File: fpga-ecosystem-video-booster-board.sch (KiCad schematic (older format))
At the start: 46 parts

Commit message: LED and I2C input option added. Annotated sch.
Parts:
- added D1: LG_L29K-G2J1-24-Z, antmicro-footprints:LED_0603, symbol antmicroLEDIndicationDiscrete:LG_L29K-G2J1-24-Z
- added R11, R12: R_15R_0402, antmicro-footprints:0402-res, symbol antmicroResistors0402:R_15R_0402
- added R4: R_330R_0402, antmicro-footprints:0402-res, symbol antmicroResistors0402:R_330R_0402
- gave numbers to parts that had none: 46
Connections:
- net labels added: SCL_MCU, SDA_MCU
- wire segments 219 -> 230
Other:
- note added: "SWD Debug"
- moved on the sheet: C1, C10, C11, C12, C13, C14, C15, C16, C17, C18, C19, C2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

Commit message: PCB update issues solved. PTN gnd connection fix
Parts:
- removed J2: HDMI_A, symbol Connector:HDMI_A
- removed J6: 685119134923, antmicro-footprints:685119134923, symbol antmicroUSBDVIHDMIConnectors:685119134923
- added J2: HDMI-PE10-19-LF, antmicro-footprints:HDMI-PE10-19-LF, symbol antmicroUSBDVIHDMIConnectors:HDMI-PE10-19-LF
- added J6: 685119134923_, antmicro-footprints:HDMI_A_Female_685119134923, symbol antmicroUSBDVIHDMIConnectors:685119134923_
- J3: footprint antmicro-footprints:PinHeader_1x4_P2.54_Drill1.1mm -> antmicro-footprints:PinHeader_1x4_P2.54mm_Drill1.02mm
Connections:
- wire segments 230 -> 238
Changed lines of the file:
@@
 Comment4 ""
 $EndDescr
-$Comp
-L Connector:HDMI_A J2
-U 1 1 5DB0BA68
-P 1650 3450
-F 0 "J2" H 2080 3496 50  0000 L CNN
-F 1 "HDMI_A" H 2080 3405 50  0000 L CNN
-F 2 "" H 1675 3450 50  0001 C CNN
-F 3 "https://en.wikipedia.org/wiki/HDMI" H 1675 3450 50  0001 C CNN
-	1    1650 3450
-	-1   0    0    -1
-$EndComp
-Text Notes 1000 3050 1    50   ~ 0
+Text Notes 1200 3400 1    50   ~ 0
 Generic\nShoud be male plus, such as \nSamtec HDMP-19-01-S-EM\nMorethanall HDMI-PE10-19-LF\n
-$Comp
-L antmicroUSBDVIHDMIConnectors:685119134923 J6
-U 1 1 5DB15BF1
-P 9400 3450
-F 0 "J6" H 9830 3496 50  0000 L CNN
-F 1 "685119134923" H 9830 3405 50  0000 L CNN
-F 2 "antmicro-footprints:685119134923" H 9425 3450 50  0001 C CNN
-F 3 "https://en.wikipedia.org/wiki/HDMI" H 9425 3450 50  0001 C CNN
-	1    9400 3450
-	1    0    0    -1
-$EndComp
-$Comp
-L antmicroInterfaceDriversReceiversTransceivers:PTN3363 U3
-U 1 1 5DB15F6D
-P 5800 3250
-F 0 "U3" H 5400 4300 60  0000 C CNN
-F 1 "PTN3363" H 6100 4300 60  0000 C CNN
-F 2 "antmicro-footprints:QFN-32-1EP_5x5mm" H 4900 1450 60  0001 L CNN
-F 3 "https://www.nxp.com/docs/en/data-sheet/PTN3363.pdf" H 4550 1350 60  0001 L CNN
-F 4 "NXP" H 5300 1550 60  0001 L CNN "Manufacturer"
-F 5 "PTN3363" H 5550 1550 60  0001 L CNN "MPN"
-	1    5800 3250
-	1    0    0    -1
-$EndComp
 $Comp
 L antmicroCapacitors0402:C_100n_0402_6V3 C12
@@
 Wire Wire Line
 	2050 2950 2950 2950
-Wire Wire Line
-	3350 3350 2050 3350
 Text Label 2150 2650 0    50   ~ 0
 IN_D2_P
@@
 	3350 3350 3350 3650
 Wire Wire Line
-	3350 3650 3950 3650
+	3350 3650 3400 3650
 Text Label 8500 2650 0    50   ~ 0
 OUT_D2_P
@@
 Wire Wire Line
 	5700 1550 5350 1550
-Wire Wire Line
-	2050 3050 3050 3050
 Wire Wire Line
 	2050 3550 2400 3550
@@
 	3250 2500 3250 3250
 Wire Wire Line
-	2050 3250 3250 3250
+	2050 3250 3000 3250
 Connection ~ 3250 3250
 Wire Wire Line
@@
 F 0 "J3" V 4541 6873 50  0000 R CNN
 F 1 "61300411121" V 4450 6873 50  0000 R CNN
-F 2 "antmicro-footprints:PinHeader_1x4_P2.54_Drill1.1mm" H 4550 7150 60  0001 L CNN
+F 2 "antmicro-footprints:PinHeader_1x4_P2.54mm_Drill1.02mm" H 4550 7150 60  0001 L CNN
 F 3 "https://katalog.we-online.de/em/datasheet/6130xx11121.pdf" H 4550 7250 60  0001 L CNN
 F 4 "61300411121" H 4550 7450 60  0001 L CNN "MPN"
@@
 	-1   0    0    -1
 $EndComp
-Wire Wire Line
-	2550 5650 2550 5750
 Connection ~ 2550 5650
 Wire Wire Line
@@
 Text Label 6200 7500 0    50   ~ 0
 SDA_SRC
+Wire Wire Line
+	2050 3350 3350 3350
+Wire Wire Line
+	2050 3050 3050 3050
+Wire Wire Line
+	2550 5650 2550 5750
+Connection ~ 2550 5750
+Wire Wire Line
+	2550 5750 2550 5850
+Connection ~ 2550 5850
+Wire Wire Line
+	2550 5850 2550 5950
+Connection ~ 2550 5950
+Wire Wire Line
+	2550 5950 2550 6050
+$Comp
+L antmicroInterfaceDriversReceiversTransceivers:PTN3363 U3
+U 1 1 5DB5B52F
+P 5800 3250
+F 0 "U3" H 5450 4300 60  0000 C CNN
+F 1 "PTN3363" H 6100 4300 60  0000 C CNN
+F 2 "antmicro-footprints:QFN-32-1EP_5x5mm" H 4900 1450 60  0001 L CNN
+F 3 "https://www.nxp.com/docs/en/data-sheet/PTN3363.pdf" H 4550 1350 60  0001 L CNN
+F 4 "NXP" H 5300 1550 60  0001 L CNN "Manufacturer"
+F 5 "PTN3363" H 5550 1550 60  0001 L CNN "MPN"
+	1    5800 3250
+	1    0    0    -1
+$EndComp
+$Comp
+L power:GND #PWR?
+U 1 1 5DB5B819
+P 6600 2450
+F 0 "#PWR?" H 6600 2200 50  0001 C CNN
+F 1 "GND" H 6605 2277 50  0000 C CNN
+F 2 "" H 6600 2450 50  0001 C CNN
+F 3 "" H 6600 2450 50  0001 C CNN
+	1    6600 2450
+	1    0    0    -1
+$EndComp
+Wire Wire Line
+	6400 2450 6600 2450
+Wire Wire Line
+	6600 2450 6600 2350
+Wire Wire Line
+	6600 2350 6400 2350
+Connection ~ 6600 2450
+$Comp
+L antmicroUSBDVIHDMIConnectors:HDMI-PE10-19-LF J2
+U 1 1 5DBAED87
+P 1550 3600
+F 0 "J2" V 1100 2850 50  0000 R CNN
+F 1 "HDMI-PE10-19-LF" V 1200 3500 50  0000 R CNN
+F 2 "antmicro-footprints:HDMI-PE10-19-LF" H 1750 3800 60  0001 L CNN
+F 3 "http://www.morethanall.com/images/products/March2017/JtPYSqVaIFqwSbTYDg6j.pdf" H 1625 3750 50  0001 C CNN
+	1    1550 3600
+	1    0    0    -1
+$EndComp
+Connection ~ 3000 3250
+Wire Wire Line
+	3000 3250 3250 3250
+Connection ~ 3400 3650
+Wire Wire Line
+	3400 3650 3950 3650
+$Comp
+L antmicroUSBDVIHDMIConnectors:685119134923_ J6
+U 1 1 5DBAFB0A
+P 9400 3450
+F 0 "J6" H 9150 4500 50  0000 L CNN
+F 1 "685119134923_" V 9900 2500 50  0000 L CNN
+F 2 "antmicro-footprints:HDMI_A_Female_685119134923" H 9600 3650 60  0001 L CNN
+F 3 "https://katalog.we-online.de/em/datasheet/685119134923.pdf" H 9425 3450 50  0001 C CNN
+	1    9400 3450
+	1    0    0    -1
+$EndComp
 $EndSCHEMATC

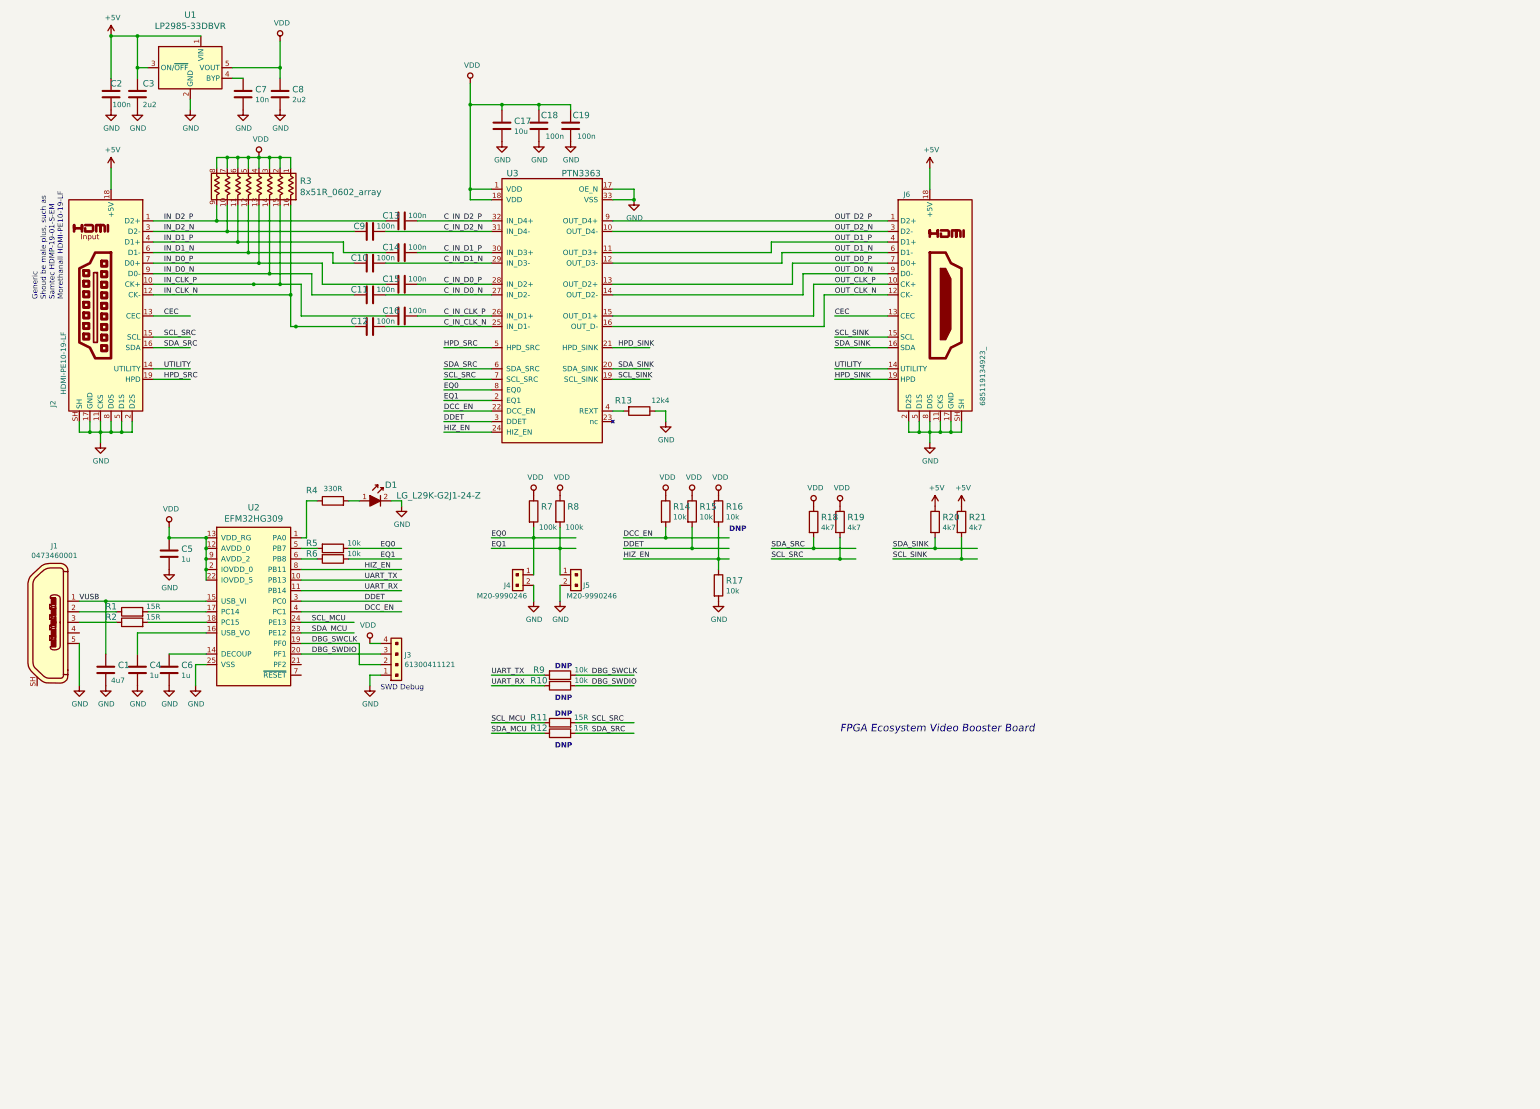
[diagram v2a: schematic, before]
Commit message: Schematics with two channels. I2Cs connected directly
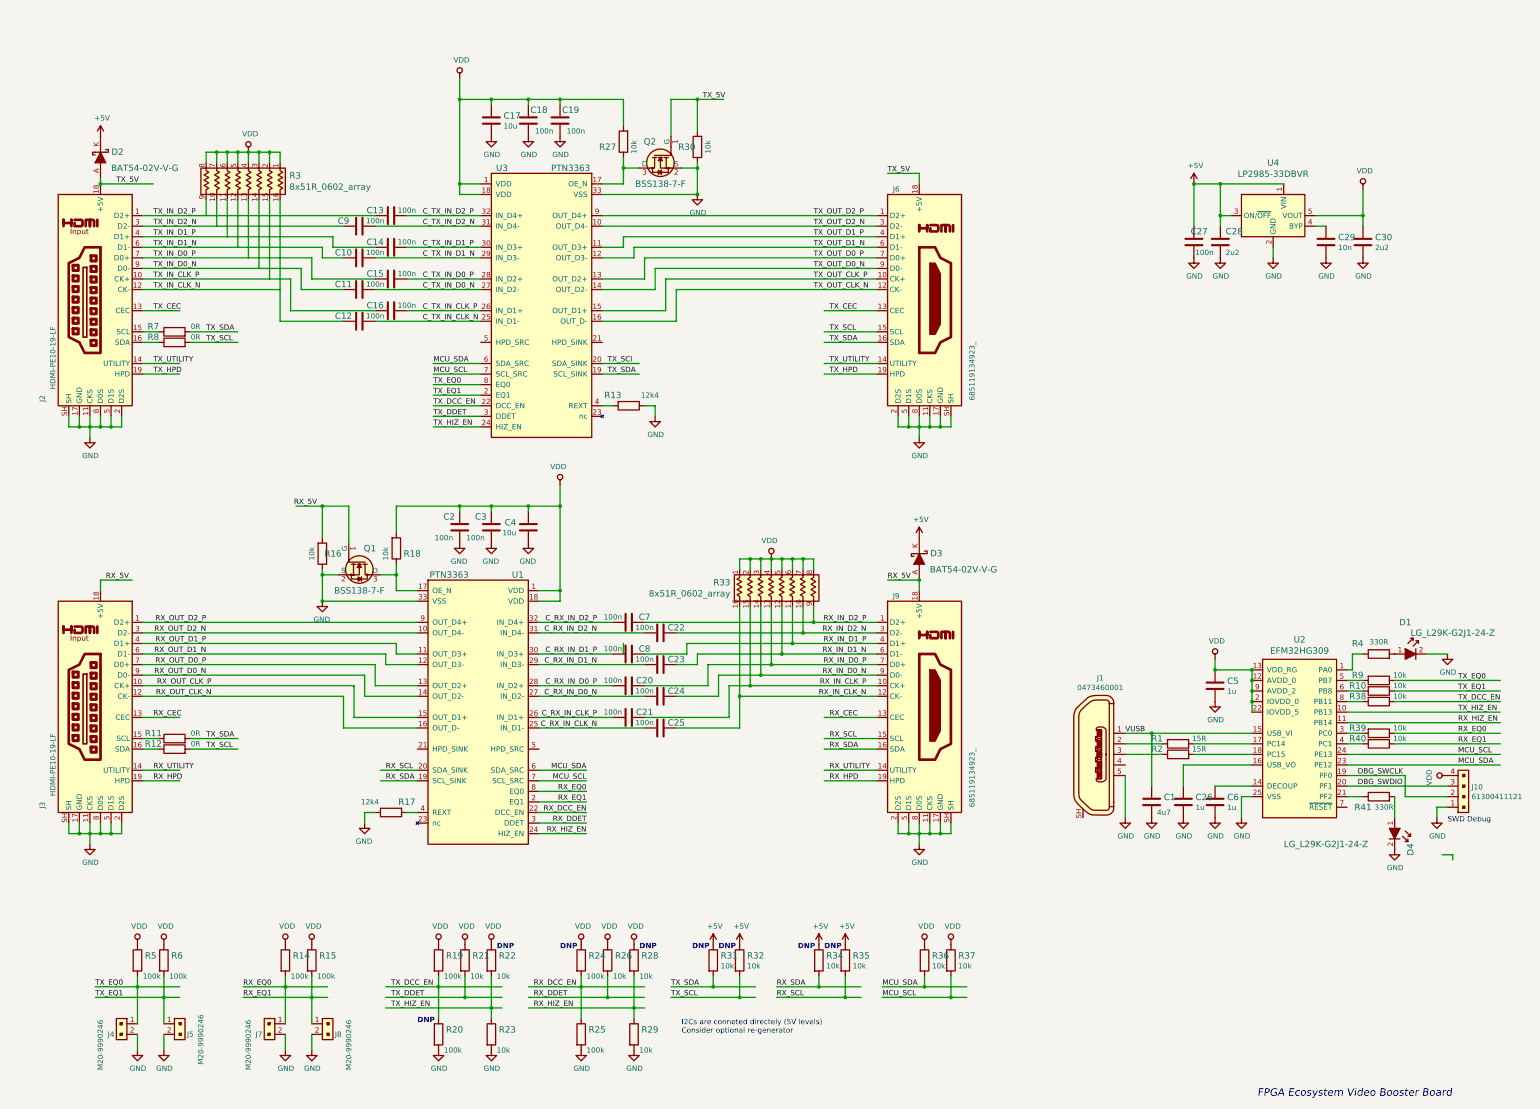
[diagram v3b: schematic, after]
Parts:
- removed C3, C8: C_2u2_0402, antmicro-footprints:0402-cap, symbol antmicroCapacitors0402:C_2u2_0402
- removed C4: C_1u_0402, antmicro-footprints:0402-cap, symbol antmicroCapacitors0402:C_1u_0402
- removed C7: C_10n_0402, antmicro-footprints:0402-cap, symbol antmicroCapacitors0402:C_10n_0402
- removed J3: 61300411121, antmicro-footprints:PinHeader_1x4_P2.54mm_Drill1.02mm, symbol antmicroRectangularConnectorsHeadersMalePins:61300411121
- removed R11, R12: R_15R_0402, antmicro-footprints:0402-res, symbol antmicroResistors0402:R_15R_0402
- removed R14, R15, R17, R5, R6: R_10k_0402, antmicro-footprints:0402-res, symbol antmicroResistors0402:R_10k_0402
- removed R18, R19, R20, R21: R_4k7_0402, antmicro-footprints:0402-res, symbol antmicroResistors0402:R_4k7_0402
- removed R7, R8: R_100k_0402, antmicro-footprints:0402-res, symbol antmicroResistors0402:R_100k_0402
- removed U1: LP2985-33DBVR, antmicro-footprints:SOT-753, symbol antmicroPMICVoltageRegulatorsLinear:LP2985-33DBVR
- added C20, C21, C22, C23, C24, C25, C27, C3, C7, C8: C_100n_0402_6V3, antmicro-footprints:0402-cap, symbol antmicroCapacitors0402:C_100n_0402_6V3
- added C26: C_1u_0402, antmicro-footprints:0402-cap, symbol antmicroCapacitors0402:C_1u_0402
- added C28, C30: C_2u2_0402, antmicro-footprints:0402-cap, symbol antmicroCapacitors0402:C_2u2_0402
- added C29: C_10n_0402, antmicro-footprints:0402-cap, symbol antmicroCapacitors0402:C_10n_0402
- added C4: C_10u_0603, antmicro-footprints:0603-cap, symbol antmicroCapacitors0603:C_10u_0603
- added D2, D3: BAT54-02V-V-G, antmicro-footprints:SOD-523, symbol antmicroDiodesRectifiersSingle:BAT54-02V-V-G
- added D4: LG_L29K-G2J1-24-Z, antmicro-footprints:LED_0603, symbol antmicroLEDIndicationDiscrete:LG_L29K-G2J1-24-Z
- added J10: 61300411121, antmicro-footprints:PinHeader_1x4_P2.54mm_Drill1.02mm, symbol antmicroRectangularConnectorsHeadersMalePins:61300411121
- added J3: HDMI-PE10-19-LF, antmicro-footprints:HDMI-PE10-19-LF, symbol antmicroUSBDVIHDMIConnectors:HDMI-PE10-19-LF
- added J7, J8: M20-9990246, antmicro-footprints:PinHeader_1x2_P2.54mm, symbol antmicroRectangularConnectorsHeadersMalePins:M20-9990246
- added J9: 685119134923_, antmicro-footprints:HDMI_A_Female_685119134923, symbol antmicroUSBDVIHDMIConnectors:685119134923_
- added Q1, Q2: BSS138-7-F, antmicro-footprints:SOT-23-3, symbol antmicroTransistorsFETsMOSFETsSingle:BSS138-7-F
- added R11, R12, R7, R8: R_0R_0402, antmicro-footprints:0402-res, symbol antmicroResistors0402:R_0R_0402
- added R14, R15, R19, R20, R24, R25, R5, R6: R_100k_0402, antmicro-footprints:0402-res, symbol antmicroResistors0402:R_100k_0402
- added R17: R_12k4_0402, antmicro-footprints:0402-res, symbol antmicroResistors0402:R_12k4_0402
- added R18, R21, R22, R23, R26, R27, R28, R29, R30, R31, R32, R34, R35, R36, R37, R38, R39, R40: R_10k_0402, antmicro-footprints:0402-res, symbol antmicroResistors0402:R_10k_0402
- added R33: 8x51R_0602_array, antmicro-footprints:R_Array_Convex_8x0602, symbol antmicroResistorNetworksArrays:8x51R_0602_array
- added R41: R_330R_0402, antmicro-footprints:0402-res, symbol antmicroResistors0402:R_330R_0402
- added U1: PTN3363, antmicro-footprints:QFN-32-1EP_5x5mm, symbol antmicroInterfaceDriversReceiversTransceivers:PTN3363
- added U4: LP2985-33DBVR, antmicro-footprints:SOT-753, symbol antmicroPMICVoltageRegulatorsLinear:LP2985-33DBVR
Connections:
- net labels added: C_RX_IN_CLK_N, C_RX_IN_CLK_P, C_RX_IN_D0_N, C_RX_IN_D0_P, C_RX_IN_D1_N, C_RX_IN_D1_P, C_RX_IN_D2_N, C_RX_IN_D2_P, C_TX_IN_CLK_N, C_TX_IN_CLK_P, C_TX_IN_D0_N, C_TX_IN_D0_P, C_TX_IN_D1_N, C_TX_IN_D1_P, C_TX_IN_D2_N, C_TX_IN_D2_P, MCU_SCL, MCU_SDA, RX_5V, RX_CEC, RX_DCC_EN, RX_DDET, RX_EQ0, RX_EQ1, RX_HIZ_EN, RX_HPD, RX_IN_CLK_N, RX_IN_CLK_P, RX_IN_D0_N, RX_IN_D0_P, RX_IN_D1_N, RX_IN_D1_P, RX_IN_D2_N, RX_IN_D2_P, RX_OUT_CLK_N, RX_OUT_CLK_P, RX_OUT_D0_N, RX_OUT_D0_P, RX_OUT_D1_N, RX_OUT_D1_P, RX_OUT_D2_N, RX_OUT_D2_P, RX_SCL, RX_SDA, RX_UTILITY, TX_5V, TX_CEC, TX_DCC_EN, TX_DDET, TX_EQ0, TX_EQ1, TX_HIZ_EN, TX_HPD, TX_IN_CLK_N, TX_IN_CLK_P, TX_IN_D0_N, TX_IN_D0_P, TX_IN_D1_N, TX_IN_D1_P, TX_IN_D2_N, TX_IN_D2_P, TX_OUT_CLK_N, TX_OUT_CLK_P, TX_OUT_D0_N, TX_OUT_D0_P, TX_OUT_D1_N, TX_OUT_D1_P, TX_OUT_D2_N, TX_OUT_D2_P, TX_SCL, TX_SCl, TX_SDA, TX_UTILITY
- net labels removed: CEC, C_IN_CLK_N, C_IN_CLK_P, C_IN_D0_N, C_IN_D0_P, C_IN_D1_N, C_IN_D1_P, C_IN_D2_N, C_IN_D2_P, DCC_EN, DDET, EQ0, EQ1, HIZ_EN, HPD_SINK, HPD_SRC, IN_CLK_N, IN_CLK_P, IN_D0_N, IN_D0_P, IN_D1_N, IN_D1_P, IN_D2_N, IN_D2_P, OUT_CLK_N, OUT_CLK_P, OUT_D0_N, OUT_D0_P, OUT_D1_N, OUT_D1_P, OUT_D2_N, OUT_D2_P, SCL_MCU, SCL_SINK, SCL_SRC, SDA_MCU, SDA_SINK, SDA_SRC, UART_RX, UART_TX, UTILITY
- wire segments 238 -> 428
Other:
- note added: "I2Cs are conneted directely (5V levels)\nConsider optional re-generator"
- note removed: "Generic\nShoud be male plus, such as \nSamtec HDMP-19-01-S-EM\nMorethanall HDMI-PE10-19-LF\n"
- moved on the sheet: C10, C11, C12, C13, C14, C15, C16, C17, C18, C19, C9, J2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
